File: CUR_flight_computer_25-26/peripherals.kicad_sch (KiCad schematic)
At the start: 19 parts, among them SW5 GSPTS0018, SW6 GSPTS0018, SW7 GSPTS0018, U7 NTR4003N

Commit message: fixed broken stuff from peripherals 2 commit
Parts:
- added R27: 22, symbol Device:R_Small_US
- renumbered BZ1 to R35
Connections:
- net +3V3: now also SW5.2, SW7.2
- net BTN_1: now also SW5.1
- net LED_2_B: now also R27.2
- net at R35.2 (-): now also D1.2 (A), U7.5 (D1)
- net at LED_2.4 (BK): now also R27.1
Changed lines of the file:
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@@
+	(wire
+		(pts
+			(xy 96.52 38.1) (xy 96.52 45.72)
+		)
+		(stroke
+			(width 0)
+			(type default)
+		)
+	)
 	(wire
 		(pts
@@
 	(wire
 		(pts
+			(xy 134.62 38.1) (xy 134.62 45.72)
+		)
+		(stroke
+			(width 0)
+			(type default)
+		)
+	)
+	(wire
+		(pts
 			(xy 88.9 129.54) (xy 88.9 127)
 		)
@@
 		(pts
 			(xy 115.57 55.88) (xy 115.57 63.5)
+		)
+		(stroke
+			(width 0)
+			(type default)
+		)
+	)
+	(wire
+		(pts
+			(xy 96.52 55.88) (xy 96.52 63.5)
 		)
 		(stroke
@@
 		(on_board yes)
 		(dnp no)
-		(fields_autoplaced yes)
-		(property "Reference" "BZ1"
-			(at 60.96 43.1799 0)
+		(property "Reference" "R35"
+			(at 65.532 41.91 0)
 			(effects
 				(font
@@
 		)
 		(property "Value" "CEM-1203(42)"
-			(at 60.96 45.7199 0)
+			(at 76.2 43.942 0)
 			(effects
 				(font
@@
 				(path "/bf7761cc-1b32-4d86-809c-5f027005229b/5946e354-b9a7-4a8a-8580-991442920c21"
 					(reference "R35")
-					(unit 1)
-				)
-			)
-		)
-	)
-	(symbol
-		(lib_id "Device:Buzzer")
-		(at 58.42 44.45 0)
-		(unit 1)
-		(exclude_from_sim no)
-		(in_bom yes)
-		(on_board yes)
-		(dnp no)
-		(fields_autoplaced yes)
-		(property "Reference" "BZ1"
-			(at 62.23 43.1799 0)
-			(effects
-				(font
-					(size 1.27 1.27)
-				)
-				(justify left)
-			)
-		)
-		(property "Value" "CEM-1203(42)"
-			(at 62.23 45.7199 0)
-			(effects
-				(font
-					(size 1.27 1.27)
-				)
-				(justify left)
-			)
-		)
-		(property "Footprint" ""
-			(at 56.515 41.91 90)
-			(effects
-				(font
-					(size 1.27 1.27)
-				)
-				(hide yes)
-			)
-		)
-		(property "Datasheet" "~"
-			(at 56.515 41.91 90)
-			(effects
-				(font
-					(size 1.27 1.27)
-				)
-				(hide yes)
-			)
-		)
-		(property "Description" "Buzzer, polarized"
-			(at 57.15 44.45 0)
-			(effects
-				(font
-					(size 1.27 1.27)
-				)
-				(hide yes)
-			)
-		)
-		(pin "2"
-		)
-		(pin "1"
-		)
-		(instances
-			(project ""
-				(path "/bf7761cc-1b32-4d86-809c-5f027005229b/5946e354-b9a7-4a8a-8580-991442920c21"
-					(reference "BZ1")
 					(unit 1)
 				)
@@
 					(unit 1)
 				)
+			)
+		)
+	)
+	(symbol
+		(lib_id "Device:R_Small_US")
+		(at 109.22 132.08 0)
+		(unit 1)
+		(exclude_from_sim no)
+		(in_bom yes)
+		(on_board yes)
+		(dnp no)
+		(property "Reference" "R27"
+			(at 103.632 129.286 90)
+			(effects
+				(font
+					(size 1.27 1.27)
+				)
+				(justify right)
+			)
+		)
+		(property "Value" "22"
+			(at 106.172 129.286 90)
+			(effects
+				(font
+					(size 1.27 1.27)
+				)
+				(justify right)
+			)
+		)
+		(property "Footprint" ""
+			(at 109.22 132.08 0)
+			(effects
+				(font
+					(size 1.27 1.27)
+				)
+				(hide yes)
+			)
+		)
+		(property "Datasheet" "~"
+			(at 109.22 132.08 0)
+			(effects
+				(font
+					(size 1.27 1.27)
+				)
+				(hide yes)
+			)
+		)
+		(property "Description" "Resistor, small US symbol"
+			(at 109.22 132.08 0)
+			(effects
+				(font
+					(size 1.27 1.27)
+				)
+				(hide yes)
+			)
+		)
+		(pin "1"
+		)
+		(pin "2"
+		)
+		(instances
+			(project "CUR_flight_computer_25-26"
+				(path "/bf7761cc-1b32-4d86-809c-5f027005229b/5946e354-b9a7-4a8a-8580-991442920c21"
+					(reference "R27")
+					(unit 1)
+				)

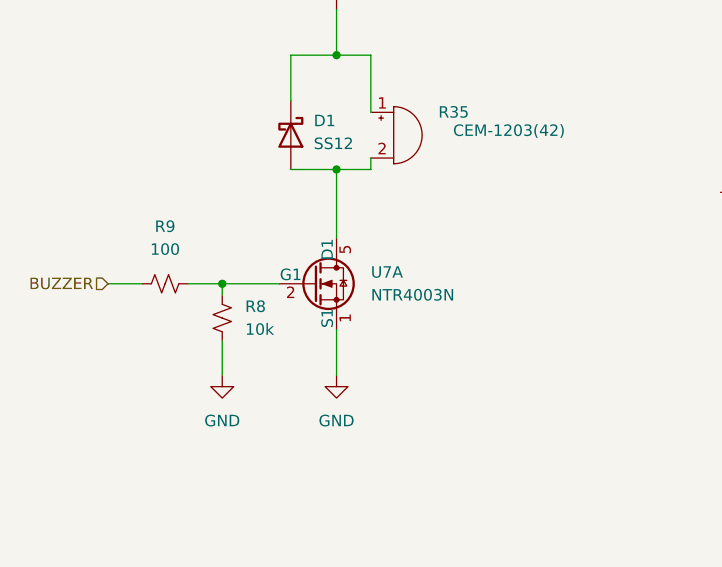
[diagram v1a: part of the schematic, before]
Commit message: Insert correct symbol for NTR4003N
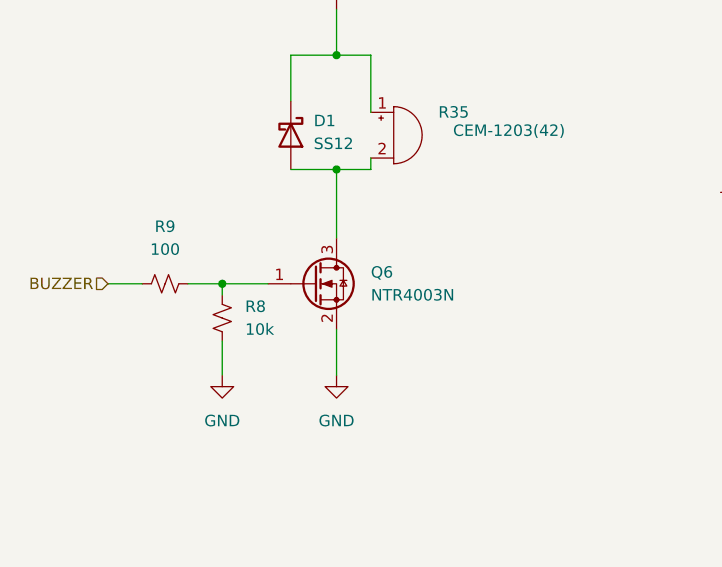
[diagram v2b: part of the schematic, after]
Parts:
- removed U7: NTR4003N, BUK9K25-40RAX:BUK9K2540RAX, symbol BUK9K25-40RAX:BUK9K25-40RAX
- added Q6: NTR4003N, Package_TO_SOT_SMD:SOT-23-3, symbol Transistor_FET:Q_NMOS_GSD
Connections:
- net GND: now also Q6.2 (S)
- net at D1.2 (A), R35.2 (-): now also Q6.3 (D)
- net at R8.1, R9.2: now also Q6.1 (G)
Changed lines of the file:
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@@
-	(wire
-		(pts
-			(xy 38.1 60.96) (xy 44.45 60.96)
-		)
-		(stroke
-			(width 0)
-			(type default)
-		)
-	)
 	(wire
 		(pts
@@
 		(pts
 			(xy 25.4 60.96) (xy 29.21 60.96)
+		)
+		(stroke
+			(width 0)
+			(type default)
+		)
+	)
+	(wire
+		(pts
+			(xy 38.1 60.96) (xy 43.18 60.96)
 		)
 		(stroke
@@
 	)
 	(symbol
-		(lib_id "BUK9K25-40RAX:BUK9K25-40RAX")
-		(at 50.8 60.96 0)
-		(unit 1)
-		(exclude_from_sim no)
-		(in_bom yes)
-		(on_board yes)
-		(dnp no)
-		(fields_autoplaced yes)
-		(property "Reference" "U7"
-			(at 54.61 59.6899 0)
-			(effects
-				(font
-					(size 1.27 1.27)
-				)
-				(justify left)
-			)
-		)
-		(property "Value" "NTR4003N"
-			(at 54.61 62.2299 0)
-			(effects
-				(font
-					(size 1.27 1.27)
-				)
-				(justify left)
-			)
-		)
-		(property "Footprint" "BUK9K25-40RAX:BUK9K2540RAX"
-			(at 50.8 60.96 0)
-			(effects
-				(font
-					(size 1.27 1.27)
-				)
-				(hide yes)
-			)
-		)
-		(property "Datasheet" "https://assets.nexperia.com/documents/data-sheet/BUK9K25-40RA.pdf"
-			(at 50.8 60.96 0)
-			(effects
-				(font
-					(size 1.27 1.27)
-				)
-				(hide yes)
-			)
-		)
-		(property "Description" "Nexperia USA Mosfet Array 40V 18.2A 2 N Channel NMOS"
-			(at 50.8 60.96 0)
-			(effects
-				(font
-					(size 1.27 1.27)
-				)
-				(hide yes)
-			)
-		)
-		(pin "5"
-		)
-		(pin "4"
-		)
-		(pin "1"
-		)
-		(pin "6"
-		)
-		(pin "3"
-		)
-		(pin "2"
-		)
-		(instances
-			(project ""
-				(path "/bf7761cc-1b32-4d86-809c-5f027005229b/5946e354-b9a7-4a8a-8580-991442920c21"
-					(reference "U7")
-					(unit 1)
-				)
-			)
-		)
-	)
-	(symbol
 		(lib_id "Device:R_Small_US")
 		(at 88.9 132.08 0)
@@
 					(unit 1)
 				)
+			)
+		)
+	)
+	(symbol
+		(lib_id "Transistor_FET:Q_NMOS_GSD")
+		(at 48.26 60.96 0)
+		(unit 1)
+		(exclude_from_sim no)
+		(in_bom yes)
+		(on_board yes)
+		(dnp no)
+		(fields_autoplaced yes)
+		(property "Reference" "Q6"
+			(at 54.61 59.6899 0)
+			(effects
+				(font
+					(size 1.27 1.27)
+				)
+				(justify left)
+			)
+		)
+		(property "Value" "NTR4003N"
+			(at 54.61 62.2299 0)
+			(effects
+				(font
+					(size 1.27 1.27)
+				)
+				(justify left)
+			)
+		)
+		(property "Footprint" "Package_TO_SOT_SMD:SOT-23-3"
+			(at 53.34 58.42 0)
+			(effects
+				(font
+					(size 1.27 1.27)
+				)
+				(hide yes)
+			)
+		)
+		(property "Datasheet" "~"
+			(at 48.26 60.96 0)
+			(effects
+				(font
+					(size 1.27 1.27)
+				)
+				(hide yes)
+			)
+		)
+		(property "Description" "N-MOSFET transistor, gate/source/drain"
+			(at 48.26 60.96 0)
+			(effects
+				(font
+					(size 1.27 1.27)
+				)
+				(hide yes)
+			)
+		)
+		(property "Sim.Library" "kicad-library-sigmondkukla\\spice\\NTR4003N.LIB"
+			(at 48.26 60.96 0)
+			(effects
+				(font
+					(size 1.27 1.27)
+				)
+				(hide yes)
+			)
+		)
+		(property "Sim.Name" "ntr4003n"
+			(at 48.26 60.96 0)
+			(effects
+				(font
+					(size 1.27 1.27)
+				)
+				(hide yes)
+			)
+		)
+		(property "Sim.Device" "SUBCKT"
+			(at 48.26 60.96 0)
+			(effects
+				(font
+					(size 1.27 1.27)
+				)
+				(hide yes)
+			)
+		)
+		(property "Sim.Pins" "1=2 2=3 3=1"
+			(at 48.26 60.96 0)
+			(effects
+				(font
+					(size 1.27 1.27)
+				)
+				(hide yes)
+			)
+		)
+		(property "MPN" "NTR4003N"
+			(at 48.26 60.96 0)
+			(effects
+				(font
+					(size 1.27 1.27)
+				)
+				(hide yes)
+			)
+		)
+		(pin "3"
+		)
+		(pin "2"
+		)
+		(pin "1"
+		)
+		(instances
+			(project "CUR_flight_computer_25-26"
+				(path "/bf7761cc-1b32-4d86-809c-5f027005229b/5946e354-b9a7-4a8a-8580-991442920c21"
+					(reference "Q6")
+					(unit 1)
+				)

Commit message: hooked up more pins
added lcd header as well
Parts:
- added J8: Conn_01x04_Pin, symbol Connector:Conn_01x04_Pin
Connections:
- net +3V3: now also J8.3 (Pin_3)
- net GND: now also J8.4 (Pin_4)
- new net LCD_SCL: J8.2 (Pin_2)
- new net LCD_SDA: J8.1 (Pin_1)
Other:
- note added: "LCD Header"

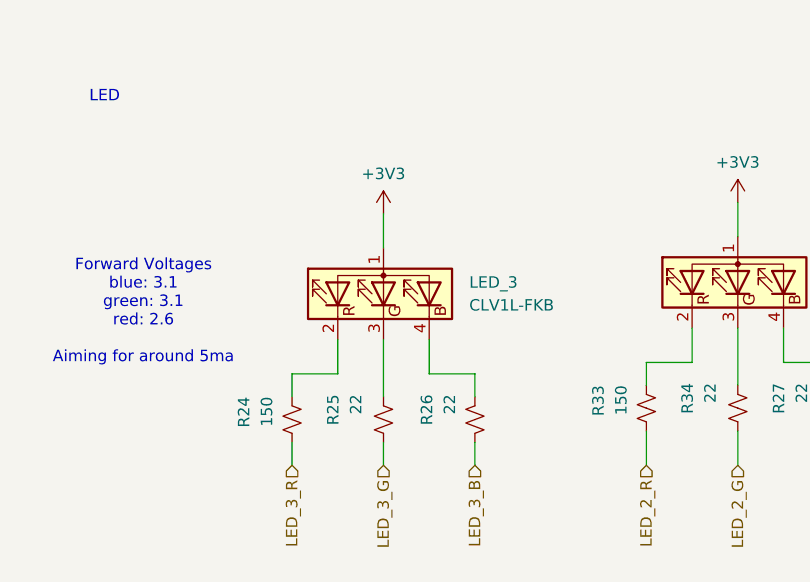
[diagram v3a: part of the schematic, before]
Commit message: updated pinout
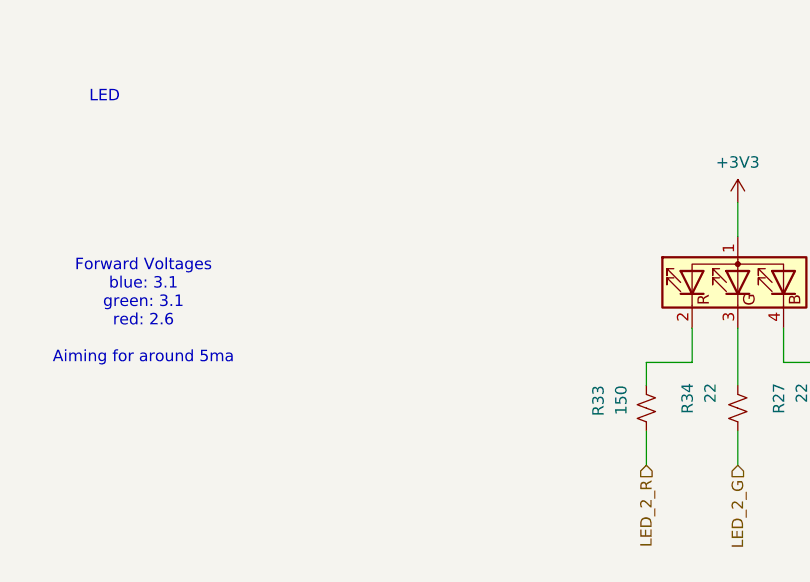
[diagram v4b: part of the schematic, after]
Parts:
- removed LED_3: CLV1L-FKB, LED_SMD:LED_Cree-PLCC4_3.2x2.8mm_CCW, symbol LED:CLV1L-FKB
- removed R24: 150, symbol Device:R_Small_US
- removed R25, R26: 22, symbol Device:R_Small_US

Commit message: updated all needed fixes
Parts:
- R48: renamed from R9; value 100 -> 150
- renumbered D1 to D17, J8 to J13, LED_2 to LED_1, LED_1 to LED_2, Q6 to Q1, R8 to R49, R35 to R50, R33 to R51, R34 to R52, R27 to R53, R30 to R54, R31 to R55, R32 to R56, SW5 to SW3, SW6 to SW4, SW7 to SW5
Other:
- moved on the sheet: J13, LED_1, LED_2, R51, R52, R53, R54, R55, R56

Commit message: assigned footrpint
need to double check:
- HSE
- Capacitors

for some unknown reason cur kicad library refuses to work
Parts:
- J13, R48, R49, R51, R52, R53, R54, R55, R56: footprint (none) -> Resistor_SMD:R_0603_1608Metric
- Q1: footprint Package_TO_SOT_SMD:SOT-23-3 -> Resistor_SMD:R_0603_1608Metric
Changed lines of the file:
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@@
 			)
 		)
-		(property "Footprint" ""
+		(property "Footprint" "Resistor_SMD:R_0603_1608Metric"
 			(at 72.39 123.19 0)
 			(effects
@@
 			)
 		)
-		(property "Footprint" ""
+		(property "Footprint" "Resistor_SMD:R_0603_1608Metric"
 			(at 176.53 38.1 0)
 			(effects
@@
 			)
 		)
-		(property "Footprint" ""
+		(property "Footprint" "Resistor_SMD:R_0603_1608Metric"
 			(at 62.23 123.19 0)
 			(effects
@@
 			)
 		)
-		(property "Footprint" ""
+		(property "Footprint" "Resistor_SMD:R_0603_1608Metric"
 			(at 102.87 123.19 0)
 			(effects
@@
 			)
 		)
-		(property "Footprint" ""
+		(property "Footprint" "Resistor_SMD:R_0603_1608Metric"
 			(at 113.03 123.19 0)
 			(effects
@@
 			)
 		)
-		(property "Footprint" ""
+		(property "Footprint" "Resistor_SMD:R_0603_1608Metric"
 			(at 123.19 123.19 0)
 			(effects
@@
 			)
 		)
-		(property "Footprint" ""
+		(property "Footprint" "Resistor_SMD:R_0603_1608Metric"
 			(at 82.55 123.19 0)
 			(effects
@@
 			)
 		)
-		(property "Footprint" "Package_TO_SOT_SMD:SOT-23-3"
+		(property "Footprint" "Resistor_SMD:R_0603_1608Metric"
 			(at 53.34 58.42 0)
 			(effects
@@
 			)
 		)
-		(property "Footprint" ""
+		(property "Footprint" "Resistor_SMD:R_0603_1608Metric"
 			(at 38.1 64.77 0)
 			(effects
@@
 			)
 		)
-		(property "Footprint" ""
+		(property "Footprint" "Resistor_SMD:R_0603_1608Metric"
 			(at 31.75 60.96 0)
 			(effects

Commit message: assigned usb footprint
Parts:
- R50: footprint (none) -> Buzzer_SameSky:Buzzer_SameSky_CEM-1203_42
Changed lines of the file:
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@@
 			)
 		)
-		(property "Footprint" ""
+		(property "Footprint" "Buzzer_SameSky:Buzzer_SameSky_CEM-1203_42"
 			(at 109.22 132.08 0)
 			(effects

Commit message: most of layout figured out
trouble finding room for power
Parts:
- J13: footprint Resistor_SMD:R_0603_1608Metric -> Connector_PinHeader_2.54mm:PinHeader_1x04_P2.54mm_Vertical
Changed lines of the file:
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@@
 			)
 		)
-		(property "Footprint" "Resistor_SMD:R_0603_1608Metric"
+		(property "Footprint" "Connector_PinHeader_2.54mm:PinHeader_1x04_P2.54mm_Vertical"
 			(at 176.53 38.1 0)
 			(effects
